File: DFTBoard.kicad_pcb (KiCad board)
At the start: 2 copper layers, 271 parts, among them CON1 AVR-JTAG-10, CON2 AVR-JTAG-10, IC1 WM8758B, IC2 IS31FL3199, IC3 CyUSB30xx-BZX, J1 JACK_TRS_6PINS, J2 JACK_TRS_6PINS, J3 JACK_TRS_6PINS, J4 JACK_TRS_6PINS, J5 MICRO_HDMI, J6 GSB3211311WEU, J7 48258-0001, Q1 IRLML2502, Q2 IRLML2502, Q3 IRLML2502, Q4 IRLML2502, Q5 IRLML2502, U1 xc7a50tftg256, U10 MAX3421, U11 GTL2002, U12 NC7WZ07P6X, U13 NC7SZ125M5X, U14 ADP198ACPZ-R7, U2 24FC128, U3 N25Q128A, U5 SC189 - 3.3V, U6 SC189 - 1.0V, U7 SC189 - 1.2V, U8 SC189 - 1.8V, U9 VL53L0X, X1 KC5032A, Y1 19.2MHz, Y2 12MHz

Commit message: a few small changes
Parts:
- moved J4 67.6 mm to (148.5, 105.0)
- moved J2 58.3 mm to (148.5, 105.0)
- moved ROT4 56.7 mm to (148.5, 105.0)
- moved J7 48.4 mm to (148.5, 105.0), turned to 0 degrees
- moved Y2 48.2 mm to (148.5, 105.0)
- moved J1 47.4 mm to (148.5, 105.0)
- moved ROT3 45.3 mm to (148.5, 105.0)
- moved C12 38.0 mm to (148.5, 105.0)
- moved ROT2 33.9 mm to (148.5, 105.0)
- moved DS1 33.8 mm to (148.5, 105.0)
- moved C21 33.3 mm to (148.5, 105.0)
- moved J3 30.6 mm to (148.5, 105.0)
- moved C24 25.0 mm to (148.5, 105.0)
- moved J6 24.0 mm to (148.5, 105.0)
- moved ROT1 22.5 mm to (148.5, 105.0)
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
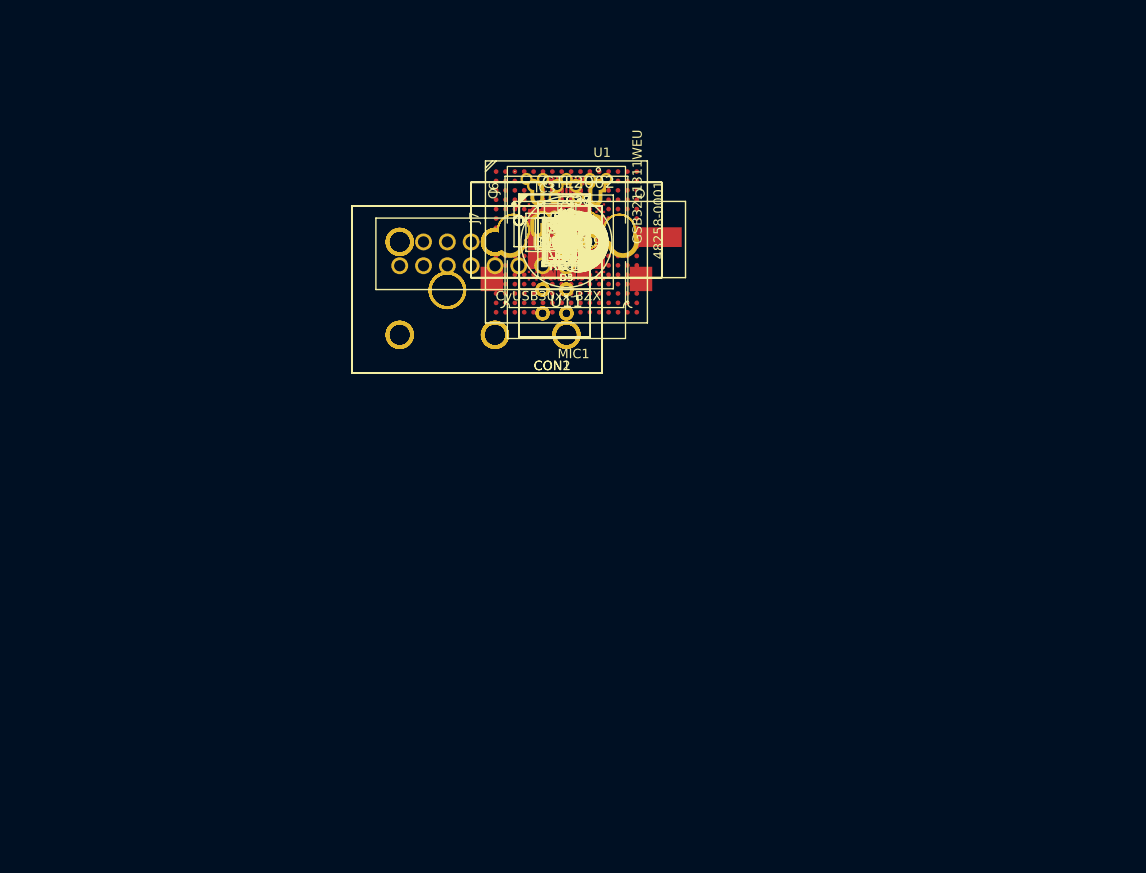
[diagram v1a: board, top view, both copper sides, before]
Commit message: fixed all schematic/footprint errors
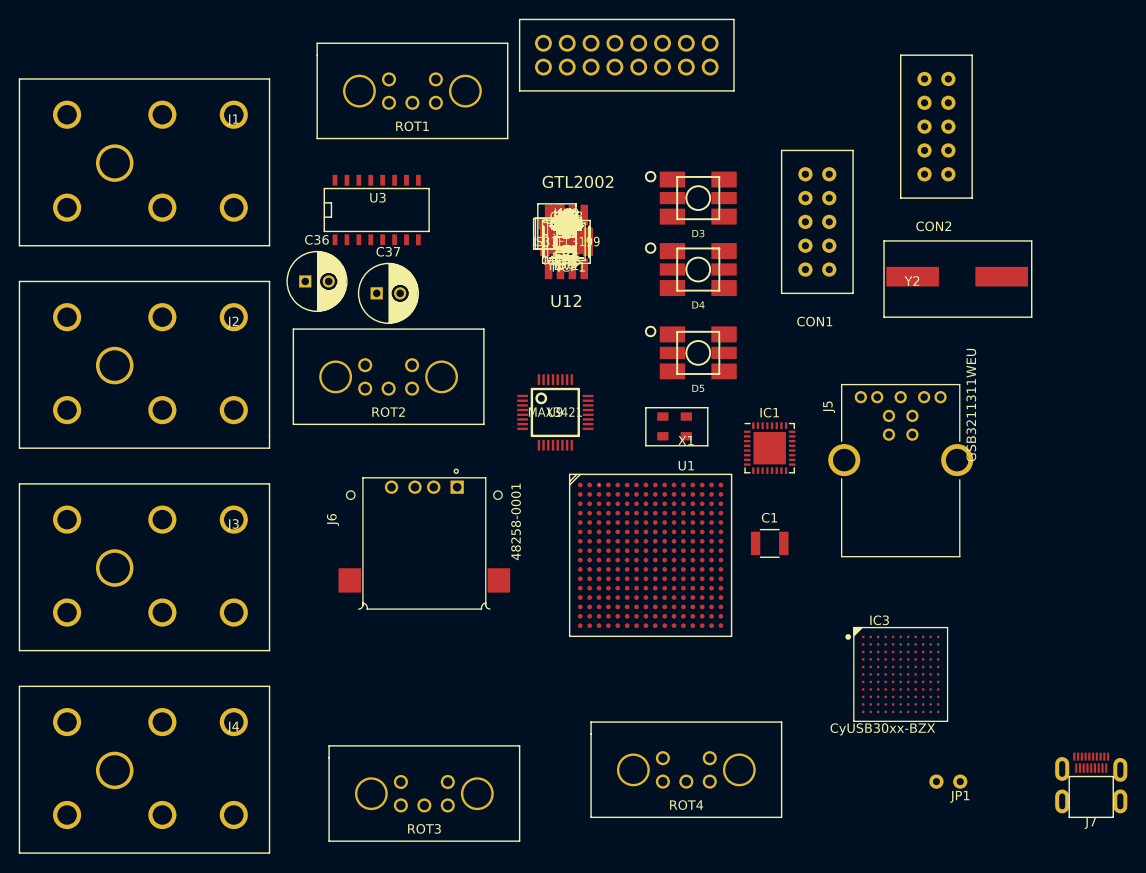
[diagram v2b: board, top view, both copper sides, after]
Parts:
- removed C126: 100nF, Capacitors_SMD:C_0603
- removed FB5: FERRITE, Diodes_SMD:D_0603
- removed R85, R86: 200, Resistors_SMD:R_1206
- removed U14: ADP198ACPZ-R7, DFTcustom:WLCSP4_P0.5mm
- added FB2: FERRITE, Diodes_SMD:D_0603, F.Cu at (148.5, 105.0)
- added U4: SC189 - 3.3V, TO_SOT_Packages_SMD:SOT-23-5, F.Cu at (148.5, 105.0)
- C100, C104: value 1uF -> .1uF
- C101: value .1uF -> 22pF; footprint Capacitors_SMD:C_0603 -> Capacitors_SMD:C_0201
- C103: value 22pF -> 1uF; footprint Capacitors_SMD:C_0201 -> Capacitors_SMD:C_0603
- C105: value .1uF -> 100nF
- C107: value 100nF -> 1nF, 250V
- C108: value 1nF, 250V -> 47uF; footprint Capacitors_SMD:C_0603 -> Capacitors_SMD:C_1210
- C109: value 47uF -> 4.7uF; footprint Capacitors_SMD:C_1210 -> Capacitors_SMD:C_0805
- C111: value 4.7uF -> .47uF; footprint Capacitors_SMD:C_0805 -> Capacitors_SMD:C_0603
- C115: value .47uF -> 100nF
- C26: value 220pF -> 4.7uF; footprint Capacitors_SMD:C_0201 -> Capacitors_SMD:C_0805
- C27, C28: value 1uF -> 4.7uF; footprint Capacitors_SMD:C_0603 -> Capacitors_SMD:C_0805
- C30: value 4.7uF -> .1uF
- C31: value .1uF -> 4.7uF
- C36: value 4.7uF -> 220uF; footprint Capacitors_SMD:C_0805 -> Capacitors_ThroughHole:C_Radial_D6.3_L11.2_P2.5
- C38: value 220uF -> .1uF; footprint Capacitors_ThroughHole:C_Radial_D6.3_L11.2_P2.5 -> Capacitors_SMD:C_0805
- C41: value .1uF -> .22uF; footprint Capacitors_SMD:C_0805 -> Capacitors_SMD:C_0402
- C43: value .22uF -> .1uF; footprint Capacitors_SMD:C_0402 -> Capacitors_SMD:C_0603
- C47, C49, C59, C70, C76, C78, C80, C84, C86: value .1uF -> .01uF; footprint Capacitors_SMD:C_0603 -> Capacitors_SMD:C_0402
- C48, C50, C60, C66, C77, C79, C85: value .01uF -> .1uF; footprint Capacitors_SMD:C_0402 -> Capacitors_SMD:C_0603
- C51: value .1uF -> 15pF; footprint Capacitors_SMD:C_0603 -> Capacitors_SMD:C_0402
- C53: value 15pF -> 2.2uF
- C54: value 2.2uF -> 22uF; footprint Capacitors_SMD:C_0402 -> Capacitors_SMD:C_0603
- C57: value 22uF -> .1uF
- C64: value .1uF -> 22uF
- C65, C74: value 22uF -> .01uF; footprint Capacitors_SMD:C_0603 -> Capacitors_SMD:C_0402
- C72, C73: value .01uF -> 0.1uF; footprint Capacitors_SMD:C_0402 -> Capacitors_SMD:C_0603
- C75: value .01uF -> 22uF; footprint Capacitors_SMD:C_0402 -> Capacitors_SMD:C_0603
- C82, C83: value 0.1uF -> .1uF
- C87: value .01uF -> 2.2uF
- C88: value 2.2uF -> .1uF; footprint Capacitors_SMD:C_0402 -> Capacitors_SMD:C_0603
- C89: value .1uF -> 10uF; footprint Capacitors_SMD:C_0603 -> Capacitors_SMD:C_0805
- C97: value 10uF -> 100nF; footprint Capacitors_SMD:C_0805 -> Capacitors_SMD:C_0603
- C98: value 100nF -> 4.7uF; footprint Capacitors_SMD:C_0603 -> Capacitors_SMD:C_0805
- C99: value 4.7uF -> 1uF; footprint Capacitors_SMD:C_0805 -> Capacitors_SMD:C_0603
- D6: value BAS16XV2T1G -> LED RED; footprint Diodes_SMD:SOD-523 -> LEDs:LED_0603
- D7: value LED RED -> LED BLUE
- D8: value LED BLUE -> BAS16XV2T1G; footprint LEDs:LED_0603 -> Diodes_SMD:SOD-523
- J1, J2, J3, J4: value JACK_TRS_6PINS -> JACK_TRS_5PINS
- J5: value MICRO_HDMI -> GSB3211311WEU; footprint DFTcustom:MICRO HDMI -> GSB3211311WEU:AMPHENOL_GSB3211311WEU
- J6: value GSB3211311WEU -> 48258-0001; footprint GSB3211311WEU:AMPHENOL_GSB3211311WEU -> 48258-0001:MOLEX_48258-0001
- J7: value 48258-0001 -> MICRO_HDMI; footprint 48258-0001:MOLEX_48258-0001 -> DFTcustom:MICRO_HDMI
- MIC1: value CMI-5247TF-K -> MEMSMIC; footprint DFTcustom:CMI-5247TF-K -> DFTcustom:WM7121PE
- NCP1: footprint UDFN-6:UDFN-6 -> DFTcustom:TSOP-5
- R2: value 270 -> 200
- R22: value 47K -> 22
- R23: value 680 -> 22
- R26: value 100k -> 50k
- R29: value 49.9k -> 100k
- R32: value 100k -> 49.9k
- R33: value 4.7k -> 100k
- R34: value 4.7k -> 50k
- R35: value 1k -> 50k
- R36: value 37.5 -> 20k
- R37: value 6.04k -> 4.7k
- R38: value 200 -> 4.7k
- R4: value 22 -> 270
- R40, R55, R58, R61: value 10k -> 1k
- R41: value 33 -> 37.5
- R42: value 33 -> 50k
- R43: value 20k -> 6.04k
- R44: value 1k -> 200
- R45, R77, R79: value 1k -> 10k
- R46: value 100k -> 10k
- R47: value 1MEG -> 1k
- R48: value 1k -> 145
- R49: value 27k -> 1k
- R5: value 22 -> 200
- R50: value 200k -> 90
- R51: value 1k -> 33
- R52: value 1.5k -> 33
- R53: value 1.5k -> 20k
- R54: value 100k -> 1k
- R56, R64: value 10k -> 100k
- R57: value 10k -> 1MEG
- R59: value 10k -> 27k
- R60: value 10k -> 200k
- R62, R63: value 10k -> 1.5k
- R75: value 20k -> 10k
- R76, R81, R82, R83: value 50k -> 10k
- R78: value 145 -> 10k
- R80: value 90 -> 10k
- U10: value MAX3421 -> NC7WZ07P6X; footprint TQFP32-5MM:TQFP32-5MM -> DFTcustom:SC-70-6
- U11: value GTL2002 -> NC7SZ125M5X; footprint DFTcustom:SO-8 -> DFTcustom:SOT-23-5
- U12: value NC7WZ07P6X -> GTL2002; footprint TO_SOT_Packages_SMD:SC-70 -> DFTcustom:SO-8
- U13: value NC7SZ125M5X -> ADP198ACPZ-R7; footprint TO_SOT_Packages_SMD:SOT-23 -> DFTcustom:LFCSP_UD
- U3: footprint DFTcustom:V-PDFN-8 6mmx5mm Sawm (MLP8) -> SMD_Packages:SO-16-N
- U5: value SC189 - 3.3V -> SC189 - 1.0V
- U6: value SC189 - 1.0V -> SC189 - 1.2V
- U7: value SC189 - 1.2V -> SC189 - 1.8V
- U8: value SC189 - 1.8V -> VL53L0X; footprint TO_SOT_Packages_SMD:SOT-23-5 -> DFTcustom:LGA12
- U9: value VL53L0X -> MAX3421; footprint DFTcustom:LGA12 -> TQFP32-5MM:TQFP32-5MM
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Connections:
- C101 pad 1: +1.8V -> AGND
- C101 pad 2: AGND -> Net-(C101-Pad2)
- C103 pad 1: AGND -> +3V3
- C103 pad 2: Net-(C103-Pad2) -> AGND
- C106 pad 1: +3V3 -> Net-(C106-Pad1)
- C107 pad 1: Net-(C107-Pad1) -> AGND
- C107 pad 2: AGND -> Net-(C107-Pad2)
- C108 pad 1: AGND -> +3V3
- C108 pad 2: Net-(C108-Pad2) -> AGND
- C26 pad 1: AGND -> Net-(C26-Pad1)
- C27 pad 1: Net-(C26-Pad2) -> +3V3
- C27 pad 2: Net-(C27-Pad2) -> AGND
- C30 pad 1: +3V3 -> JD_IN
- C31 pad 1: JD_IN -> +1.8V
- C33 pad 1: +1.8V -> Net-(C33-Pad1)
- C34 pad 2: Net-(C34-Pad2) -> AGND
- C36 pad 1: MICBIAS -> Net-(C36-Pad1)
- C36 pad 2: AGND -> Net-(C36-Pad2)
- C38 pad 1: Net-(C38-Pad1) -> JD_ROUT
- C38 pad 2: Net-(C38-Pad2) -> AGND
- C39 pad 1: JD_ROUT -> JD_LOUT
- C40 pad 1: JD_LOUT -> JD_HOUT
- C41 pad 1: JD_HOUT -> Net-(C41-Pad1)
- C41 pad 2: AGND -> AUDIO_IN
- C43 pad 1: Net-(C43-Pad1) -> +3V3
- C43 pad 2: AUDIO_IN -> AGND
- C44 pad 1: +3V3 -> Net-(C44-Pad1)
- C45 pad 1: Net-(C45-Pad1) -> +5V
- C47 pad 1: +5V -> +1.8V
- C51 pad 1: +1.8V -> Net-(C51-Pad1)
- C53 pad 1: Net-(C53-Pad1) -> +1.2V
- C57 pad 1: +1.2V -> CVDDQ
- C58 pad 1: CVDDQ -> +1.2V
- C59 pad 1: +1.2V -> CVDDQ
- C60 pad 1: CVDDQ -> +1.2V
- C61 pad 1: +1.2V -> Net-(C61-Pad1)
- C62 pad 1: Net-(C62-Pad1) -> +1.8V
- C63 pad 1: +1.8V -> +1.2V
- C64 pad 1: +1.2V -> Net-(C61-Pad1)
- C65 pad 1: Net-(C62-Pad1) -> +1.8V
- C66 pad 1: +1.8V -> +1.2V
- C67 pad 1: +1.2V -> +3V3
- C68 pad 1: +3V3 -> Net-(C68-Pad1)
- C69 pad 1: Net-(C69-Pad1) -> +1.8V
- C70 pad 1: +1.8V -> +1.2V
- C71 pad 1: +1.2V -> +3V3
- C72 pad 1: +3V3 -> Net-(C72-Pad1)
- C72 pad 2: AGND -> Net-(C72-Pad2)
- C73 pad 1: +1.2V -> Net-(C73-Pad1)
- C73 pad 2: AGND -> Net-(C73-Pad2)
- C74 pad 1: Net-(C69-Pad1) -> +1.2V
- C75 pad 1: +1.8V -> Net-(C68-Pad1)
- C77 pad 1: +1.2V -> +1.8V
- C78 pad 1: +1.8V -> +1.2V
- C80 pad 1: +1.2V -> +1.8V
- C81 pad 1: Net-(C81-Pad1) -> +1.2V
- C82 pad 2: Net-(C82-Pad2) -> AGND
- C83 pad 1: Net-(C83-Pad1) -> +5V
- C83 pad 2: Net-(C83-Pad2) -> AGND
- C84 pad 1: +5V -> +1.8V
- C86 pad 1: +1.8V -> +1.2V
- C87 pad 1: +1.2V -> Net-(C82-Pad1)
- C88 pad 1: Net-(C81-Pad1) -> +1.2V
- C89 pad 1: +1.2V -> +5V
- C91 pad 1: +5V -> +3V3
- C92 pad 1: +3V3 -> +1.0V
- C93 pad 1: +1.0V -> +5V
- C95 pad 1: +5V -> +1.2V
- C96 pad 1: +1.2V -> +1.8V
- C97 pad 1: +1.8V -> +3V3
- C99 pad 1: +3V3 -> +1.8V
- F1 pad 1: (no net) -> Net-(F1-Pad1)
- F1 pad 2: (no net) -> HDMI_5V0
- FB3 pad 2: Net-(C62-Pad1) -> Net-(C68-Pad1)
- FB4 pad 2: Net-(C69-Pad1) -> Net-(C82-Pad1)
- IC1 pad 19: Net-(IC1-Pad19) -> Net-(C33-Pad1)
- IC1 pad 20: Net-(C34-Pad2) -> Net-(C28-Pad2)
- IC1 pad 23: Net-(C38-Pad1) -> Net-(C37-Pad1)
- IC1 pad 25: Net-(C37-Pad1) -> Net-(C36-Pad1)
- IC1 pad 27: Net-(C35-Pad1) -> Net-(C34-Pad1)
- IC1 pad 32: MICBIAS -> Net-(C35-Pad1)
- IC1 pad 4: Net-(C27-Pad2) -> Net-(C26-Pad1)
- IC1 pad 5: Net-(C28-Pad2) -> AGND
- IC2 pad 17: Net-(C43-Pad1) -> Net-(C41-Pad1)
- IC2 pad 2: Net-(C45-Pad1) -> Net-(C44-Pad1)
- IC3 pad A2: Net-(C62-Pad1) -> Net-(C61-Pad1)
- IC3 pad A5: Net-(C83-Pad2) -> Net-(C73-Pad2)
- IC3 pad A6: Net-(C82-Pad2) -> Net-(C72-Pad2)
- IC3 pad A7: Net-(C81-Pad1) -> Net-(C82-Pad1)
- IC3 pad B5: Net-(C69-Pad1) -> Net-(C68-Pad1)
- IC3 pad C6: Net-(C52-Pad1) -> Net-(C51-Pad1)
- IC3 pad C7: Net-(C53-Pad1) -> Net-(C52-Pad1)
- J1 pad R: (no net) -> Net-(IC1-Pad2)
- J1 pad RB: (no net) -> Net-(IC1-Pad2)
- J1 pad S: (no net) -> AGND
- J1 pad T: (no net) -> Net-(IC1-Pad1)
- J1 pad TB: (no net) -> Net-(J1-PadTB)
- J2 pad R: (no net) -> Net-(C37-Pad2)
- J2 pad RB: (no net) -> Net-(J2-PadRB)
- J2 pad S: (no net) -> AGND
- J2 pad T: (no net) -> Net-(C36-Pad2)
- J2 pad TB: (no net) -> Net-(C36-Pad2)
- J3 pad R: (no net) -> AGND
- J3 pad RB: (no net) -> AGND
- J3 pad S: (no net) -> AGND
- J3 pad T: (no net) -> Net-(IC1-Pad29)
- J3 pad TB: (no net) -> Net-(J3-PadTB)
- J4 pad R: (no net) -> AGND
- J4 pad RB: (no net) -> AGND
- J4 pad S: (no net) -> AGND
- J4 pad T: (no net) -> Net-(IC1-Pad30)
- J4 pad TB: (no net) -> Net-(J4-PadTB)
- J5 pad 1: Net-(J5-Pad1) -> +5V
- J5 pad 2: Net-(J5-Pad2) -> Net-(IC3-PadA10)
- J5 pad 3: Net-(J5-Pad3) -> Net-(IC3-PadA9)
- J5 pad 5: Net-(J5-Pad5) -> Net-(C72-Pad1)
- J5 pad 6: Net-(J5-Pad6) -> Net-(C73-Pad1)
- J5 pad 8: Net-(J5-Pad8) -> Net-(IC3-PadA3)
- J5 pad 9: Net-(J5-Pad9) -> Net-(IC3-PadA4)
- J6 pad 1: +5V -> Net-(J6-Pad1)
- J6 pad 2: Net-(IC3-PadA10) -> Net-(J6-Pad2)
- J6 pad 3: Net-(IC3-PadA9) -> Net-(J6-Pad3)
- MIC1 pad 1: AGND -> +3V3
- MIC1 pad 2: Net-(C26-Pad2) -> AGND
- Q1 pad 2: AGND -> Net-(Q1-Pad2)
- Q1 pad 3: Net-(DS1-Pad16) -> +3V3
- Q2 pad 2: AGND -> Net-(Q2-Pad2)
- Q2 pad 3: Net-(D7-Pad1) -> +3V3
- Q3 pad 3: Net-(D8-Pad1) -> Net-(DS1-Pad16)
- Q4 pad 2: Net-(Q4-Pad2) -> AGND
- Q4 pad 3: +3V3 -> Net-(D6-Pad1)
- Q5 pad 2: Net-(Q5-Pad2) -> AGND
- Q5 pad 3: +3V3 -> Net-(D7-Pad1)
- R1 pad 2: Net-(Q4-Pad2) -> Net-(Q1-Pad2)
- R10 pad 2: GD_10 -> GD_2
- R11 pad 2: GD_14 -> GD_6
- R12 pad 2: GA_1 -> GD_10
- R13 pad 2: GD_1 -> GD_14
- R14 pad 2: GD_5 -> GA_1
- R15 pad 2: GD_9 -> GD_1
- R16 pad 2: GD_13 -> GD_5
- R17 pad 2: GA_0 -> GD_9
- R18 pad 2: GD_0 -> GD_13
- R19 pad 2: GD_4 -> GA_0
- R2 pad 1: Net-(D2-Pad2) -> Net-(Q1-Pad1)
- R2 pad 2: Net-(Q5-Pad2) -> CONFIG_DONE
- R20 pad 2: GD_8 -> GD_0
- R21 pad 2: GD_12 -> GD_4
- R22 pad 1: Net-(C26-Pad2) -> Net-(R22-Pad1)
- R22 pad 2: AGND -> GD_8
- R23 pad 1: MICBIAS -> Net-(R23-Pad1)
- R23 pad 2: Net-(C26-Pad2) -> GD_12
- R24 pad 2: Net-(J1-Pad5) -> Net-(J1-PadTB)
- R25 pad 2: Net-(J1-Pad5) -> Net-(J1-PadTB)
- R26 pad 1: Net-(J2-Pad5) -> +1.8V
- R26 pad 2: +3V3 -> Net-(IC1-Pad15)
- R27 pad 1: Net-(J3-Pad5) -> Net-(J3-PadTB)
- R28 pad 1: Net-(J4-Pad6) -> Net-(J4-PadTB)
- R29 pad 1: JD_ROUT -> Net-(J2-PadRB)
- R29 pad 2: Net-(J2-Pad5) -> +3V3
- R30 pad 1: JD_LOUT -> JD_ROUT
- R30 pad 2: Net-(J3-Pad5) -> Net-(J3-PadTB)
- R31 pad 1: JD_HOUT -> JD_LOUT
- R31 pad 2: Net-(J4-Pad6) -> Net-(J4-PadTB)
- R32 pad 1: Net-(IC2-Pad15) -> JD_HOUT
- R32 pad 2: AGND -> Net-(J2-PadRB)
- R33 pad 1: I2C_SCLK -> Net-(IC2-Pad15)
- R33 pad 2: +1.8V -> AGND
- R34 pad 1: I2C_SDIN -> Net-(IC2-Pad16)
- R34 pad 2: +1.8V -> AGND
- R35 pad 1: Net-(Q1-Pad1) -> Net-(R35-Pad1)
- R35 pad 2: PWM_LCD_DIM -> +1.8V
- R36 pad 1: Net-(DS1-Pad15) -> +1.8V
- R36 pad 2: +5V -> Net-(R36-Pad2)
- R37 pad 1: Net-(IC3-PadC8) -> I2C_SCLK
- R37 pad 2: AGND -> +1.8V
- R38 pad 1: Net-(IC3-PadB3) -> I2C_SDIN
- R38 pad 2: AGND -> +1.8V
- R39 pad 2: RF_SD -> Net-(IC3-PadH4)
- R4 pad 1: Net-(R4-Pad1) -> Net-(D2-Pad2)
- R4 pad 2: GD_3 -> Net-(Q2-Pad2)
- R40 pad 1: +1.8V -> Net-(Q3-Pad1)
- R40 pad 2: RF_IRQ -> PWM_LCD_DIM
- R41 pad 1: Net-(J7-Pad2) -> Net-(DS1-Pad15)
- R41 pad 2: Net-(R41-Pad2) -> +5V
- R42 pad 1: Net-(J7-Pad3) -> CVDDQ
- R42 pad 2: Net-(R42-Pad2) -> Net-(IC3-PadC5)
- R43 pad 1: +5V -> Net-(IC3-PadC8)
- R43 pad 2: USB_FAULT -> AGND
- R44 pad 1: +3V3 -> Net-(IC3-PadB3)
- R44 pad 2: HDMI_SCL -> AGND
- R45 pad 1: +3V3 -> +1.8V
- R45 pad 2: HDMI_SDA -> RF_SD
- R46 pad 1: Net-(J5-Pad1) -> +1.8V
- R46 pad 2: AGND -> RF_IRQ
- R47 pad 1: AGND -> Net-(Q4-Pad1)
- R47 pad 2: Net-(C108-Pad2) -> Net-(R47-Pad2)
- R48 pad 1: Net-(R48-Pad1) -> Net-(D6-Pad2)
- R48 pad 2: Net-(J5-Pad1) -> +5V
- R49 pad 1: Net-(D6-Pad1) -> Net-(Q5-Pad1)
- R49 pad 2: +3V3 -> Net-(R49-Pad2)
- R5 pad 1: Net-(R5-Pad1) -> Net-(Q2-Pad1)
- R5 pad 2: GD_7 -> CONFIG_INIT
- R50 pad 1: HDMI_5V0 -> Net-(D7-Pad2)
- R50 pad 2: Net-(C107-Pad1) -> +5V
- R51 pad 1: Net-(R51-Pad1) -> Net-(J6-Pad2)
- R52 pad 1: HDMI_5V0 -> Net-(J6-Pad3)
- R52 pad 2: Net-(J5-Pad17) -> Net-(R52-Pad2)
- R53 pad 1: HDMI_5V0 -> +5V
- R53 pad 2: Net-(J5-Pad18) -> USB_FAULT
- R54 pad 1: Net-(R51-Pad1) -> +3V3
- R54 pad 2: AGND -> HDMI_SCL
- R55 pad 1: +1.8V -> +3V3
- R55 pad 2: ENCC0_SW -> HDMI_SDA
- R56 pad 1: +1.8V -> Net-(J7-Pad1)
- R56 pad 2: ENCC2_SW -> AGND
- R57 pad 1: +1.8V -> AGND
- R57 pad 2: Net-(R57-Pad2) -> Net-(C107-Pad2)
- R58 pad 1: +1.8V -> Net-(R58-Pad1)
- R58 pad 2: Net-(R58-Pad2) -> Net-(J7-Pad1)
- R59 pad 1: +1.8V -> Net-(D8-Pad1)
- R59 pad 2: Net-(R59-Pad2) -> +3V3
- R6 pad 2: GD_11 -> GD_3
- R60 pad 1: +1.8V -> HDMI_5V0
- R60 pad 2: Net-(R60-Pad2) -> Net-(C106-Pad1)
- R61 pad 1: ENCC0_Q0 -> Net-(R61-Pad1)
- R61 pad 2: Net-(R57-Pad2) -> Net-(R61-Pad2)
- R62 pad 1: ENCC0_Q1 -> HDMI_5V0
- R62 pad 2: Net-(R59-Pad2) -> Net-(J7-Pad17)
- R63 pad 1: ENCC2_Q0 -> HDMI_5V0
- R63 pad 2: Net-(R58-Pad2) -> Net-(J7-Pad18)
- R64 pad 1: ENCC2_Q1 -> Net-(R61-Pad1)
- R64 pad 2: Net-(R60-Pad2) -> AGND
- R65 pad 2: ENCC1_SW -> ENCC0_SW
- R66 pad 1: +3V3 -> +1.8V
- R66 pad 2: ENCC3_SW -> ENCC2_SW
- R68 pad 1: +3V3 -> +1.8V
- R7 pad 2: GD_15 -> GD_7
- R70 pad 1: +3V3 -> +1.8V
- R71 pad 1: ENCC1_Q0 -> ENCC0_Q0
- R72 pad 1: ENCC1_Q1 -> ENCC0_Q1
- R73 pad 1: ENCC3_Q0 -> ENCC2_Q0
- R74 pad 1: ENCC3_Q1 -> ENCC2_Q1
- R75 pad 2: Net-(R75-Pad2) -> ENCC1_SW
- R76 pad 1: CVDDQ -> +3V3
- R76 pad 2: Net-(IC3-PadC5) -> ENCC3_SW
- R77 pad 1: Net-(Q2-Pad1) -> +1.8V
- R78 pad 1: Net-(D7-Pad2) -> +3V3
- R78 pad 2: +5V -> Net-(R78-Pad2)
- R79 pad 1: Net-(Q3-Pad1) -> +1.8V
- R8 pad 2: GD_2 -> GD_11
- R80 pad 1: Net-(D8-Pad2) -> +3V3
- R80 pad 2: +5V -> Net-(R80-Pad2)
- R81 pad 1: +1.8V -> ENCC1_Q0
- R81 pad 2: Net-(IC1-Pad15) -> Net-(R77-Pad2)
- R82 pad 1: Net-(R82-Pad1) -> ENCC1_Q1
- R82 pad 2: +1.8V -> Net-(R79-Pad2)
- R83 pad 1: Net-(IC2-Pad16) -> ENCC3_Q0
- R83 pad 2: AGND -> Net-(R78-Pad2)
- R84 pad 1: +1.8V -> ENCC3_Q1
- R84 pad 2: Net-(IC3-PadH4) -> Net-(R80-Pad2)
- R9 pad 2: GD_6 -> GD_15
- ROT1 pad A: (no net) -> Net-(R67-Pad2)
- ROT1 pad B: (no net) -> Net-(R69-Pad2)
- ROT1 pad C: (no net) -> AGND
- ROT1 pad S1: (no net) -> ENCC0_SW
- ROT1 pad S2: (no net) -> AGND
- ROT2 pad A: (no net) -> Net-(R68-Pad2)
- ROT2 pad B: (no net) -> Net-(R70-Pad2)
- ROT2 pad C: (no net) -> AGND
- ROT2 pad S1: (no net) -> ENCC2_SW
- ROT2 pad S2: (no net) -> AGND
- ROT3 pad A: (no net) -> Net-(R77-Pad2)
- ROT3 pad B: (no net) -> Net-(R79-Pad2)
- ROT3 pad C: (no net) -> AGND
- ROT3 pad S1: (no net) -> ENCC1_SW
- ROT3 pad S2: (no net) -> AGND
- ROT4 pad A: (no net) -> Net-(R78-Pad2)
- ROT4 pad B: (no net) -> Net-(R80-Pad2)
- ROT4 pad C: (no net) -> AGND
- ROT4 pad S1: (no net) -> ENCC3_SW
- ROT4 pad S2: (no net) -> AGND
- U1 pad A3: Net-(J5-Pad11) -> Net-(J7-Pad11)
- U1 pad A7: Net-(J5-Pad8) -> Net-(J7-Pad8)
- U1 pad B4: Net-(J5-Pad9) -> Net-(J7-Pad9)
- U1 pad B5: Net-(J5-Pad5) -> Net-(J7-Pad5)
- U1 pad B6: Net-(J5-Pad3) -> Net-(J7-Pad3)
- U1 pad B7: Net-(J5-Pad6) -> Net-(J7-Pad6)
- U1 pad C6: Net-(D6-Pad2) -> Net-(D8-Pad2)
- U1 pad C7: Net-(R51-Pad1) -> Net-(R61-Pad1)
- U1 pad E5: Net-(J5-Pad14) -> Net-(J7-Pad14)
- U1 pad F5: Net-(J5-Pad12) -> Net-(J7-Pad12)
- U1 pad K13: Net-(R5-Pad1) -> Net-(R7-Pad1)
- U1 pad K15: Net-(R13-Pad1) -> Net-(R15-Pad1)
- U1 pad K16: Net-(R18-Pad1) -> Net-(R20-Pad1)
- U1 pad L12: Net-(R15-Pad1) -> Net-(R17-Pad1)
- U1 pad L13: Net-(R9-Pad1) -> Net-(R11-Pad1)
- U1 pad L14: Net-(R14-Pad1) -> Net-(R16-Pad1)
- U1 pad L15: Net-(R4-Pad1) -> Net-(R6-Pad1)
- U1 pad M12: Net-(R20-Pad1) -> Net-(R22-Pad1)
- U1 pad M14: Net-(R19-Pad1) -> Net-(R21-Pad1)
- U1 pad M15: Net-(R8-Pad1) -> Net-(R10-Pad1)
- U1 pad M16: Net-(R6-Pad1) -> Net-(R8-Pad1)
- U1 pad N13: Net-(R12-Pad1) -> Net-(R14-Pad1)
- U1 pad N16: Net-(R10-Pad1) -> Net-(R12-Pad1)
- U1 pad P13: Net-(R17-Pad1) -> Net-(R19-Pad1)
- U1 pad P15: Net-(R16-Pad1) -> Net-(R18-Pad1)
- U1 pad P16: Net-(R21-Pad1) -> Net-(R23-Pad1)
- U1 pad R15: Net-(R7-Pad1) -> Net-(R9-Pad1)
- U1 pad R16: Net-(R11-Pad1) -> Net-(R13-Pad1)
- U10 pad 1: ENCC2_Q1 -> Net-(J7-Pad1)
- U10 pad 2: +1.8V -> AGND
- U10 pad 3: AGND -> Net-(U10-Pad3)
- U10 pad 4: LED_SD -> Net-(U10-Pad4)
- U10 pad 5: RF_SD -> +3V3
- U10 pad 6: I2CMEM_WP -> Net-(R61-Pad2)
- U11 pad 1: AGND -> HDMI_OUT_EN
- U11 pad 2: +3V3 -> Net-(R61-Pad1)
- U11 pad 3: HDMI_SCL -> AGND
- U11 pad 4: HDMI_SDA -> Net-(R58-Pad1)
- U11 pad 5: Net-(J5-Pad18) -> +3V3
- U12 pad 1: Net-(J5-Pad1) -> AGND
- U12 pad 2: (no net) -> +3V3
- U12 pad 3: (no net) -> HDMI_SCL
- U13 pad 1: HDMI_OUT_EN -> Net-(F1-Pad1)
- U13 pad 2: Net-(R51-Pad1) -> Net-(F1-Pad1)
- U13 pad 3: (no net) -> AGND
- U3 pad 1: Net-(R82-Pad1) -> Net-(R35-Pad1)
- U5 pad 4: +3V3 -> +1.0V
- U5 pad 5: Net-(L1-Pad1) -> Net-(L2-Pad1)
- U6 pad 4: +1.0V -> +1.2V
- U6 pad 5: Net-(L2-Pad1) -> Net-(L3-Pad1)
- U7 pad 4: +1.2V -> +1.8V
- U7 pad 5: Net-(L3-Pad1) -> Net-(L4-Pad1)
- U8 pad 1: +5V -> +3V3
- U8 pad 3: +5V -> AGND
- U8 pad 4: +1.8V -> AGND
- U8 pad 5: Net-(L4-Pad1) -> RF_SD
- U9 pad 1: +3V3 -> ENCC2_Q1
- U9 pad 10: I2C_SCLK -> Net-(R49-Pad2)
- U9 pad 11: +3V3 -> Net-(U9-Pad11)
- U9 pad 12: AGND -> +1.8V
- U9 pad 2: AGND -> +1.8V
- U9 pad 4: AGND -> LED_SD
- U9 pad 6: AGND -> I2CMEM_WP
- U9 pad 7: RF_IRQ -> CONFIG_INIT
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
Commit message: started PCBnew trivial connections and BGA interface, shuffled some net connections, etc.
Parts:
- removed C36, C37: 220uF, Capacitors_ThroughHole:C_Radial_D6.3_L11.2_P2.5
- removed D8: BAS16XV2T1G, Diodes_SMD:SOD-523
- added Q6: IRLML2502, TO_SOT_Packages_SMD:SOT-23, F.Cu at (74.8, 50.2)
- added R85: 10k, Resistors_SMD:R_1206, F.Cu at (142.2, 75.0)
- added R86: 10k, Resistors_SMD:R_1206, F.Cu at (137.8, 76.2)
- added R87: 10k, Resistors_SMD:R_1206, F.Cu at (148.3, 78.6)
- added R88: 10k, Resistors_SMD:R_1206, F.Cu at (135.1, 82.0)
- added R89: 10k, Resistors_SMD:R_1206, F.Cu at (141.2, 70.1)
- added R90: 10k, Resistors_SMD:R_1206, F.Cu at (127.2, 74.7)
- added R91: 10k, Resistors_SMD:R_1206, F.Cu at (134.6, 70.9)
- added R92: 10k, Resistors_SMD:R_1206, F.Cu at (141.8, 83.4)
- added R93: 10k, Resistors_SMD:R_1206, F.Cu at (129.9, 79.8)
- added SW1: SW_IL, DFTcustom:tl6215_right_angle, F.Cu at (74.0, 38.5)
- C10, C11, C12, C13, C14, C15, C16, C17, C18, C19, C20, C21, C22, C23, C24, C25, C9, DS1, NCP1, U9: moved to B.Cu
- C63: value .1uF -> 0.1uF
- C64: value 22uF -> 0.1uF
- C65, C70, C71: value .01uF -> .1uF; footprint Capacitors_SMD:C_0402 -> Capacitors_SMD:C_0603
- C66: value .1uF -> 22uF
- C67: value .1uF -> .01uF; footprint Capacitors_SMD:C_0603 -> Capacitors_SMD:C_0402
- C72, C73: value 0.1uF -> .01uF; footprint Capacitors_SMD:C_0603 -> Capacitors_SMD:C_0402
- IC3: footprint CYUSB3014-BZXCT:BGA121C80P11X11_1000X1000X110 -> DFTcustom:BGA121_08mm
- R1: value 60 -> 200
- R10, R11, R12, R13, R14, R15, R16, R17, R18, R19, R20, R21, R22, R23, R6, R7, R8, R9: footprint Resistors_SMD:R_1206 -> Resistors_SMD:R_0201
- R2: value 200 -> 60
- R24, R27, R28, R29: value 100k -> 22; footprint Resistors_SMD:R_1206 -> Resistors_SMD:R_0201
- R25, R30, R31: value 49.9k -> 22; footprint Resistors_SMD:R_1206 -> Resistors_SMD:R_0201
- R26: value 50k -> 22; footprint Resistors_SMD:R_1206 -> Resistors_SMD:R_0201
- R3: value 4.7k -> 270
- R32: value 49.9k -> 100k
- R33: value 100k -> 49.9k
- R35: value 50k -> 100k
- R36: value 20k -> 100k
- R37: value 4.7k -> 100k
- R38: value 4.7k -> 49.9k
- R39: value 10k -> 49.9k
- R4: value 270 -> 200
- R40: value 1k -> 49.9k
- R41: value 37.5 -> 100k
- R43: value 6.04k -> 50k
- R44: value 200 -> 20k
- R45, R46: value 10k -> 4.7k
- R47, R54: value 1k -> 10k
- R48: value 145 -> 1k
- R49: value 1k -> 37.5
- R5: value 200 -> 4.7k
- R50: value 90 -> 50k
- R51: value 33 -> 6.04k
- R52: value 33 -> 200
- R53: value 20k -> 10k
- R56: value 100k -> 145
- R57: value 1MEG -> 1k
- R58: value 1k -> 90
- R59: value 27k -> 20k
- R60: value 200k -> 33; moved to B.Cu
- R61: value 1k -> 33; moved to B.Cu
- R62: value 1.5k -> 20k
- R63: value 1.5k -> 1k
- R64: value 100k -> 1k
- R65, R73: value 10k -> 100k
- R66: value 10k -> 1MEG
- R67, R70: value 10k -> 1k
- R68: value 10k -> 27k
- R69: value 10k -> 200k
- R71, R72: value 10k -> 1.5k
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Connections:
- net Net-(C51-Pad1) renamed /Cypress FX3/XP
- net Net-(C52-Pad1) renamed /Cypress FX3/XN
- net Net-(C82-Pad1) renamed /Cypress FX3/AVDD
- net Net-(CON1-Pad1) renamed AX_TCLK
- net Net-(CON1-Pad3) renamed AX_TDO
- net Net-(CON1-Pad5) renamed AX_TMS
- net Net-(CON1-Pad9) renamed AX_TDI
- net Net-(CON2-Pad1) renamed FX_TCK
- net Net-(CON2-Pad3) renamed FX_TDO
- net Net-(CON2-Pad5) renamed FX_TMS
- net Net-(CON2-Pad8) renamed FX_nTRST
- net Net-(CON2-Pad9) renamed FX_TDI
- net Net-(D8-Pad2) renamed HDMI_CEC
- net Net-(DS1-Pad11) renamed LCD_D4
- net Net-(DS1-Pad12) renamed LCD_D5
- net Net-(DS1-Pad13) renamed LCD_D6
- net Net-(DS1-Pad14) renamed LCD_D7
- net Net-(DS1-Pad4) renamed LCD_RS
- net Net-(DS1-Pad6) renamed LCD_E
- net Net-(IC3-PadA10) renamed FXD_N
- net Net-(IC3-PadA9) renamed FXD_P
- net Net-(J6-Pad1) renamed SPIUSB_VBUS
- net Net-(J7-Pad11) renamed TMDS_DAT0_N
- net Net-(J7-Pad12) renamed TMDS_CLK_P
- net Net-(J7-Pad14) renamed TMDS_CLK_N
- net Net-(J7-Pad3) renamed TMDS_DAT2_P
- net Net-(J7-Pad5) renamed TMDS_DAT2_N
- net Net-(J7-Pad6) renamed TMDS_DAT1_P
- net Net-(J7-Pad8) renamed TMDS_DAT1_N
- net Net-(J7-Pad9) renamed TMDS_DAT0_P
- C107 pad 2: Net-(C107-Pad2) -> /HDMI/HDMI_SHD
- C61 pad 1: Net-(C61-Pad1) -> /Cypress FX3/U3RXVDDQ
- C63 pad 1: +1.2V -> SSTX_N
- C63 pad 2: AGND -> /Cypress FX3/SSTXAC_N
- C64 pad 1: Net-(C61-Pad1) -> SSTX_P
- C64 pad 2: AGND -> /Cypress FX3/SSTXAC_P
- C65 pad 1: +1.8V -> +1.2V
- C66 pad 1: +1.2V -> /Cypress FX3/U3RXVDDQ
- C67 pad 1: +3V3 -> +1.8V
- C68 pad 1: Net-(C68-Pad1) -> +1.2V
- C69 pad 1: +1.8V -> +3V3
- C70 pad 1: +1.2V -> /Cypress FX3/U3TXVDDQ
- C71 pad 1: +3V3 -> +1.8V
- C72 pad 1: Net-(C72-Pad1) -> +1.2V
- C72 pad 2: Net-(C72-Pad2) -> AGND
- C73 pad 1: Net-(C73-Pad1) -> +3V3
- C73 pad 2: Net-(C73-Pad2) -> AGND
- C75 pad 1: Net-(C68-Pad1) -> /Cypress FX3/U3TXVDDQ
- CON1 pad 6: Net-(CON1-Pad6) -> (no net)
- CON1 pad 7: Net-(CON1-Pad7) -> (no net)
- CON1 pad 8: Net-(CON1-Pad8) -> (no net)
- CON2 pad 6: Net-(CON2-Pad6) -> (no net)
- CON2 pad 7: Net-(CON2-Pad7) -> (no net)
- D1 pad 1: AGND -> Net-(D1-Pad1)
- D2 pad 1: AGND -> Net-(D2-Pad1)
- DS1 pad 10: Net-(DS1-Pad10) -> (no net)
- DS1 pad 7: Net-(DS1-Pad7) -> (no net)
- DS1 pad 8: Net-(DS1-Pad8) -> (no net)
- DS1 pad 9: Net-(DS1-Pad9) -> (no net)
- FB2 pad 2: Net-(C61-Pad1) -> /Cypress FX3/U3RXVDDQ
- FB3 pad 2: Net-(C68-Pad1) -> /Cypress FX3/U3TXVDDQ
- IC1 pad 21: Net-(IC1-Pad21) -> (no net)
- IC1 pad 23: Net-(C37-Pad1) -> (no net)
- IC1 pad 25: Net-(C36-Pad1) -> (no net)
- IC1 pad 3: Net-(IC1-Pad3) -> (no net)
- IC1 pad 6: Net-(IC1-Pad6) -> (no net)
- IC2 pad 14: Net-(IC2-Pad14) -> (no net)
- IC2 pad 20: Net-(IC2-Pad20) -> (no net)
- IC3 pad A11: Net-(IC3-PadA11) -> (no net)
- IC3 pad A2: Net-(C61-Pad1) -> /Cypress FX3/U3RXVDDQ
- IC3 pad A3: Net-(IC3-PadA3) -> SSRX_N
- IC3 pad A4: Net-(IC3-PadA4) -> SSRX_P
- IC3 pad A5: Net-(C73-Pad2) -> /Cypress FX3/SSTXAC_P
- IC3 pad A6: Net-(C72-Pad2) -> /Cypress FX3/SSTXAC_N
- IC3 pad B3: Net-(IC3-PadB3) -> /Cypress FX3/RUSB3
- IC3 pad B5: Net-(C68-Pad1) -> /Cypress FX3/U3TXVDDQ
- IC3 pad C5: Net-(IC3-PadC5) -> /Cypress FX3/nRESET
- IC3 pad C8: Net-(IC3-PadC8) -> /Cypress FX3/RUSB2
- IC3 pad C9: Net-(IC3-PadC9) -> (no net)
- IC3 pad D11: Net-(IC3-PadD11) -> (no net)
- IC3 pad D6: Net-(IC3-PadD6) -> (no net)
- IC3 pad D7: Net-(IC3-PadD7) -> (no net)
- IC3 pad E10: Net-(IC3-PadE10) -> (no net)
- IC3 pad L4: Net-(IC3-PadL4) -> (no net)
- IC3 pad L8: Net-(IC3-PadL8) -> (no net)
- J2 pad R: Net-(C37-Pad2) -> (no net)
- J5 pad 5: Net-(C72-Pad1) -> SSTX_N
- J5 pad 6: Net-(C73-Pad1) -> SSTX_P
- J5 pad 8: Net-(IC3-PadA3) -> SSRX_P
- J5 pad 9: Net-(IC3-PadA4) -> SSRX_N
- J6 pad 2: Net-(J6-Pad2) -> SPIUSB_D_N
- J6 pad 3: Net-(J6-Pad3) -> SPIUSB_D_P
- J7 pad 2: Net-(J7-Pad2) -> (no net)
- J7 pad SHD: Net-(C107-Pad2) -> /HDMI/HDMI_SHD
- Q1 pad 2: Net-(Q1-Pad2) -> AGND
- Q1 pad 3: +3V3 -> Net-(D1-Pad1)
- Q2 pad 2: Net-(Q2-Pad2) -> AGND
- Q2 pad 3: +3V3 -> Net-(D2-Pad1)
- Q3 pad 1: Net-(Q3-Pad1) -> TEMPO_LED
- Q3 pad 3: Net-(DS1-Pad16) -> (no net)
- Q4 pad 3: Net-(D6-Pad1) -> Net-(DS1-Pad16)
- Q5 pad 3: Net-(D7-Pad1) -> Net-(D6-Pad1)
- R1 pad 1: Net-(D1-Pad2) -> Net-(Q1-Pad1)
- R1 pad 2: Net-(Q1-Pad2) -> CONFIG_DONE
- R10 pad 1: Net-(R10-Pad1) -> GPIF_PCLKT
- R10 pad 2: GD_2 -> GPIF_PCLK
- R11 pad 1: Net-(R11-Pad1) -> GPIF_FLAGAT
- R11 pad 2: GD_6 -> GPIF_FLAGA
- R12 pad 1: Net-(R12-Pad1) -> GD_2T
- R12 pad 2: GD_10 -> GD_2
- R13 pad 1: Net-(R13-Pad1) -> GD_6T
- R13 pad 2: GD_14 -> GD_6
- R14 pad 1: Net-(R14-Pad1) -> GD_10T
- R14 pad 2: GA_1 -> GD_10
- R15 pad 1: Net-(R15-Pad1) -> GD_14T
- R15 pad 2: GD_1 -> GD_14
- R16 pad 1: Net-(R16-Pad1) -> GPIF_SLOE#T
- R16 pad 2: GD_5 -> GPIF_SLOE#
- R17 pad 1: Net-(R17-Pad1) -> GPIF_FLAGBT
- R17 pad 2: GD_9 -> GPIF_FLAGB
- R18 pad 1: Net-(R18-Pad1) -> GD_1T
- R18 pad 2: GD_13 -> GD_1
- R19 pad 1: Net-(R19-Pad1) -> GD_5T
- R19 pad 2: GA_0 -> GD_5
- R2 pad 1: Net-(Q1-Pad1) -> Net-(D1-Pad2)
- R2 pad 2: CONFIG_DONE -> +3V3
- R20 pad 1: Net-(R20-Pad1) -> GD_9T
- R20 pad 2: GD_0 -> GD_9
- R21 pad 1: Net-(R21-Pad1) -> GD_13T
- R21 pad 2: GD_4 -> GD_13
- R22 pad 1: Net-(R22-Pad1) -> GA_1T
- R22 pad 2: GD_8 -> GA_1
- R23 pad 1: Net-(R23-Pad1) -> GPIF_SLRD#T
- R23 pad 2: GD_12 -> GPIF_SLRD#
- R24 pad 1: +1.8V -> GPIF_PKTEND#T
- R24 pad 2: Net-(J1-PadTB) -> GPIF_PKTEND#
- R25 pad 1: JD_IN -> GD_0T
- R25 pad 2: Net-(J1-PadTB) -> GD_0
- R26 pad 1: +1.8V -> GD_4T
- R26 pad 2: Net-(IC1-Pad15) -> GD_4
- R27 pad 1: Net-(J3-PadTB) -> GD_8T
- R27 pad 2: +3V3 -> GD_8
- R28 pad 1: Net-(J4-PadTB) -> GD_12T
- R28 pad 2: +3V3 -> GD_12
- R29 pad 1: Net-(J2-PadRB) -> GA_0T
- R29 pad 2: +3V3 -> GA_0
- R3 pad 1: +1.8V -> Net-(D2-Pad2)
- R3 pad 2: CONFIG_INIT -> +3V3
- R30 pad 1: JD_ROUT -> GPIF_SLWR#T
- R30 pad 2: Net-(J3-PadTB) -> GPIF_SLWR#
- R31 pad 1: JD_LOUT -> GPIF_SLCS#T
- R31 pad 2: Net-(J4-PadTB) -> GPIF_SLCS#
- R32 pad 1: JD_HOUT -> +1.8V
- R32 pad 2: Net-(J2-PadRB) -> Net-(J1-PadTB)
- R33 pad 1: Net-(IC2-Pad15) -> JD_IN
- R33 pad 2: AGND -> Net-(J1-PadTB)
- R34 pad 1: Net-(IC2-Pad16) -> +1.8V
- R34 pad 2: AGND -> Net-(IC1-Pad15)
- R35 pad 1: Net-(R35-Pad1) -> Net-(J3-PadTB)
- R35 pad 2: +1.8V -> +3V3
- R36 pad 1: +1.8V -> Net-(J4-PadTB)
- R36 pad 2: Net-(R36-Pad2) -> +3V3
- R37 pad 1: I2C_SCLK -> Net-(J2-PadRB)
- R37 pad 2: +1.8V -> +3V3
- R38 pad 1: I2C_SDIN -> JD_ROUT
- R38 pad 2: +1.8V -> Net-(J3-PadTB)
- R39 pad 1: +1.8V -> JD_LOUT
- R39 pad 2: Net-(IC3-PadH4) -> Net-(J4-PadTB)
- R4 pad 1: Net-(D2-Pad2) -> CONFIG_INIT
- R4 pad 2: Net-(Q2-Pad2) -> Net-(Q2-Pad1)
- R40 pad 1: Net-(Q3-Pad1) -> JD_HOUT
- R40 pad 2: PWM_LCD_DIM -> Net-(J2-PadRB)
- R41 pad 1: Net-(DS1-Pad15) -> Net-(IC2-Pad15)
- R41 pad 2: +5V -> AGND
- R42 pad 1: CVDDQ -> Net-(IC2-Pad16)
- R42 pad 2: Net-(IC3-PadC5) -> AGND
- R43 pad 1: Net-(IC3-PadC8) -> Net-(R43-Pad1)
- R43 pad 2: AGND -> +1.8V
- R44 pad 1: Net-(IC3-PadB3) -> +1.8V
- R44 pad 2: AGND -> Net-(R44-Pad2)
- R45 pad 1: +1.8V -> I2C_SCLK
- R45 pad 2: RF_SD -> +1.8V
- R46 pad 1: +1.8V -> I2C_SDIN
- R46 pad 2: RF_IRQ -> +1.8V
- R47 pad 1: Net-(Q4-Pad1) -> +1.8V
- R47 pad 2: Net-(R47-Pad2) -> Net-(IC3-PadH4)
- R48 pad 1: Net-(D6-Pad2) -> Net-(Q4-Pad1)
- R48 pad 2: +5V -> PWM_LCD_DIM
- R49 pad 1: Net-(Q5-Pad1) -> Net-(DS1-Pad15)
- R49 pad 2: Net-(R49-Pad2) -> +5V
- R5 pad 1: Net-(Q2-Pad1) -> CONFIG_INIT
- R5 pad 2: CONFIG_INIT -> +1.8V
- R50 pad 1: Net-(D7-Pad2) -> CVDDQ
- R50 pad 2: +5V -> /Cypress FX3/nRESET
- R51 pad 1: Net-(J6-Pad2) -> /Cypress FX3/RUSB2
- R51 pad 2: Net-(R51-Pad2) -> AGND
- R52 pad 1: Net-(J6-Pad3) -> /Cypress FX3/RUSB3
- R52 pad 2: Net-(R52-Pad2) -> AGND
- R53 pad 1: +5V -> +1.8V
- R53 pad 2: USB_FAULT -> RF_SD
- R54 pad 1: +3V3 -> +1.8V
- R54 pad 2: HDMI_SCL -> RF_IRQ
- R55 pad 1: +3V3 -> Net-(Q5-Pad1)
- R55 pad 2: HDMI_SDA -> Net-(R55-Pad2)
- R56 pad 1: Net-(J7-Pad1) -> Net-(D6-Pad2)
- R56 pad 2: AGND -> +5V
- R57 pad 1: AGND -> Net-(Q6-Pad1)
- R57 pad 2: Net-(C107-Pad2) -> Net-(R57-Pad2)
- R58 pad 1: Net-(R58-Pad1) -> Net-(D7-Pad2)
- R58 pad 2: Net-(J7-Pad1) -> +5V
- R59 pad 1: Net-(D8-Pad1) -> +1.8V
- R59 pad 2: +3V3 -> Net-(R59-Pad2)
- R6 pad 1: Net-(R6-Pad1) -> GD_3T
- R60 pad 1: HDMI_5V0 -> SPIUSB_D_P
- R60 pad 2: Net-(C106-Pad1) -> /SPIUSBBRIDGE/SPIUSB_DT_P
- R61 pad 1: Net-(R61-Pad1) -> SPIUSB_D_N
- R61 pad 2: Net-(R61-Pad2) -> /SPIUSBBRIDGE/SPIUSB_DT_N
- R62 pad 1: HDMI_5V0 -> +5V
- R62 pad 2: Net-(J7-Pad17) -> USB_FAULT
- R63 pad 1: HDMI_5V0 -> +3V3
- R63 pad 2: Net-(J7-Pad18) -> HDMI_SCL
- R64 pad 1: Net-(R61-Pad1) -> +3V3
- R64 pad 2: AGND -> HDMI_SDA
- R65 pad 1: +1.8V -> Net-(J7-Pad1)
- R65 pad 2: ENCC0_SW -> AGND
- R66 pad 1: +1.8V -> AGND
- R66 pad 2: ENCC2_SW -> /HDMI/HDMI_SHD
- R67 pad 1: +1.8V -> Net-(R67-Pad1)
- R67 pad 2: Net-(R67-Pad2) -> Net-(J7-Pad1)
- R68 pad 1: +1.8V -> (no net)
- R68 pad 2: Net-(R68-Pad2) -> +3V3
- R69 pad 1: +1.8V -> HDMI_5V0
- R69 pad 2: Net-(R69-Pad2) -> Net-(C106-Pad1)
- R7 pad 1: Net-(R7-Pad1) -> GD_7T
- R70 pad 1: +1.8V -> HDMI_DETECT
- R71 pad 1: ENCC0_Q0 -> HDMI_5V0
- R71 pad 2: Net-(R67-Pad2) -> Net-(J7-Pad17)
- R72 pad 1: ENCC0_Q1 -> HDMI_5V0
- R72 pad 2: Net-(R69-Pad2) -> Net-(J7-Pad18)
- R73 pad 1: ENCC2_Q0 -> HDMI_DETECT
- R73 pad 2: Net-(R68-Pad2) -> AGND
- R74 pad 1: ENCC2_Q1 -> +1.8V
- R74 pad 2: Net-(R70-Pad2) -> ENCC0_SW
- R75 pad 2: ENCC1_SW -> ENCC2_SW
- R76 pad 1: +3V3 -> +1.8V
- R76 pad 2: ENCC3_SW -> Net-(R76-Pad2)
- R78 pad 1: +3V3 -> +1.8V
- R8 pad 1: Net-(R8-Pad1) -> GD_11T
- R80 pad 1: +3V3 -> ENCC0_Q0
- R80 pad 2: Net-(R80-Pad2) -> Net-(R76-Pad2)
- R81 pad 1: ENCC1_Q0 -> ENCC0_Q1
- R81 pad 2: Net-(R77-Pad2) -> Net-(R78-Pad2)
- R82 pad 1: ENCC1_Q1 -> ENCC2_Q0
- R82 pad 2: Net-(R79-Pad2) -> Net-(R77-Pad2)
- R83 pad 1: ENCC3_Q0 -> ENCC2_Q1
- R83 pad 2: Net-(R78-Pad2) -> Net-(R79-Pad2)
- R84 pad 1: ENCC3_Q1 -> +1.8V
- R84 pad 2: Net-(R80-Pad2) -> ENCC1_SW
- R9 pad 1: Net-(R9-Pad1) -> GD_15T
- ROT1 pad A: Net-(R67-Pad2) -> Net-(R76-Pad2)
- ROT1 pad B: Net-(R69-Pad2) -> Net-(R78-Pad2)
- ROT2 pad A: Net-(R68-Pad2) -> Net-(R77-Pad2)
- ROT2 pad B: Net-(R70-Pad2) -> Net-(R79-Pad2)
- ROT3 pad A: Net-(R77-Pad2) -> Net-(R86-Pad2)
- ROT3 pad B: Net-(R79-Pad2) -> Net-(R88-Pad2)
- ROT4 pad A: Net-(R78-Pad2) -> Net-(R87-Pad2)
- ROT4 pad B: Net-(R80-Pad2) -> Net-(R89-Pad2)
- U1 pad A10: Net-(U1-PadA10) -> (no net)
- U1 pad A12: Net-(U1-PadA12) -> (no net)
- U1 pad A13: Net-(U1-PadA13) -> (no net)
- U1 pad A14: Net-(U1-PadA14) -> (no net)
- U1 pad A15: Net-(U1-PadA15) -> (no net)
- U1 pad A2: Net-(U1-PadA2) -> (no net)
- U1 pad A4: Net-(U1-PadA4) -> (no net)
- U1 pad A5: Net-(U1-PadA5) -> (no net)
- U1 pad A8: Net-(U1-PadA8) -> (no net)
- U1 pad A9: Net-(U1-PadA9) -> (no net)
- U1 pad B1: Net-(U1-PadB1) -> (no net)
- U1 pad B10: Net-(U1-PadB10) -> (no net)
- U1 pad B11: Net-(U1-PadB11) -> (no net)
- U1 pad B12: Net-(U1-PadB12) -> (no net)
- U1 pad B14: Net-(U1-PadB14) -> (no net)
- U1 pad B15: Net-(U1-PadB15) -> (no net)
- U1 pad B16: Net-(U1-PadB16) -> (no net)
- U1 pad B2: Net-(U1-PadB2) -> (no net)
- U1 pad B9: Net-(U1-PadB9) -> (no net)
- U1 pad C1: Net-(U1-PadC1) -> (no net)
- U1 pad C11: Net-(U1-PadC11) -> (no net)
- U1 pad C12: Net-(U1-PadC12) -> (no net)
- U1 pad C13: Net-(U1-PadC13) -> (no net)
- U1 pad C14: Net-(U1-PadC14) -> (no net)
- U1 pad C16: Net-(U1-PadC16) -> (no net)
- U1 pad C2: Net-(U1-PadC2) -> (no net)
- U1 pad C3: Net-(U1-PadC3) -> (no net)
- U1 pad C7: Net-(R61-Pad1) -> HDMI_DETECT
- U1 pad C8: Net-(U1-PadC8) -> (no net)
- U1 pad C9: Net-(U1-PadC9) -> (no net)
- U1 pad D1: Net-(U1-PadD1) -> (no net)
- U1 pad D10: Net-(U1-PadD10) -> (no net)
- U1 pad D11: Net-(U1-PadD11) -> (no net)
- U1 pad D13: Net-(U1-PadD13) -> (no net)
- U1 pad D14: Net-(U1-PadD14) -> (no net)
- U1 pad D15: Net-(U1-PadD15) -> (no net)
- U1 pad D16: Net-(U1-PadD16) -> (no net)
- U1 pad D3: Net-(U1-PadD3) -> (no net)
- U1 pad D4: Net-(U1-PadD4) -> (no net)
- U1 pad D6: Net-(U1-PadD6) -> (no net)
- U1 pad D8: Net-(U1-PadD8) -> (no net)
- U1 pad D9: Net-(U1-PadD9) -> (no net)
- U1 pad E1: Net-(U1-PadE1) -> (no net)
- U1 pad E11: Net-(U1-PadE11) -> (no net)
- U1 pad E12: Net-(U1-PadE12) -> (no net)
- U1 pad E13: Net-(U1-PadE13) -> (no net)
- U1 pad E15: Net-(U1-PadE15) -> (no net)
- U1 pad E16: Net-(U1-PadE16) -> (no net)
- U1 pad E2: Net-(U1-PadE2) -> (no net)
- U1 pad E3: Net-(U1-PadE3) -> (no net)
- U1 pad E6: Net-(U1-PadE6) -> (no net)
- U1 pad F12: Net-(U1-PadF12) -> (no net)
- U1 pad F13: Net-(U1-PadF13) -> (no net)
- U1 pad F14: Net-(U1-PadF14) -> (no net)
- U1 pad F15: Net-(U1-PadF15) -> (no net)
- U1 pad F2: Net-(U1-PadF2) -> (no net)
- U1 pad F3: Net-(U1-PadF3) -> (no net)
- U1 pad F4: Net-(U1-PadF4) -> (no net)
- U1 pad G1: Net-(U1-PadG1) -> (no net)
- U1 pad G11: Net-(U1-PadG11) -> (no net)
- U1 pad G12: Net-(U1-PadG12) -> (no net)
- U1 pad G14: Net-(U1-PadG14) -> (no net)
- U1 pad G15: Net-(U1-PadG15) -> (no net)
- U1 pad G16: Net-(U1-PadG16) -> (no net)
- U1 pad G2: Net-(U1-PadG2) -> (no net)
- U1 pad H1: Net-(U1-PadH1) -> (no net)
- U1 pad H11: Net-(U1-PadH11) -> (no net)
- U1 pad H12: Net-(U1-PadH12) -> (no net)
- U1 pad H13: Net-(U1-PadH13) -> (no net)
- U1 pad H14: Net-(U1-PadH14) -> (no net)
- U1 pad H16: Net-(U1-PadH16) -> (no net)
- U1 pad H2: Net-(U1-PadH2) -> (no net)
- U1 pad H3: Net-(U1-PadH3) -> (no net)
- U1 pad H4: Net-(U1-PadH4) -> (no net)
- U1 pad H5: Net-(U1-PadH5) -> (no net)
- U1 pad J1: Net-(U1-PadJ1) -> (no net)
- U1 pad J13: GPIF_FLAGA -> GPIF_FLAGAT
- U1 pad J14: GPIF_FLAGB -> GPIF_FLAGBT
- U1 pad J15: Net-(U1-PadJ15) -> (no net)
- U1 pad J16: Net-(U1-PadJ16) -> (no net)
- U1 pad J3: Net-(U1-PadJ3) -> (no net)
- U1 pad J4: Net-(U1-PadJ4) -> (no net)
- U1 pad J5: Net-(U1-PadJ5) -> (no net)
- U1 pad K1: Net-(U1-PadK1) -> (no net)
- U1 pad K12: GPIF_SLCS# -> GPIF_SLCS#T
- U1 pad K13: Net-(R7-Pad1) -> GD_10T
- U1 pad K15: Net-(R15-Pad1) -> GD_13T
- U1 pad K16: Net-(R20-Pad1) -> GD_11T
- U1 pad K2: Net-(U1-PadK2) -> (no net)
- U1 pad K3: Net-(U1-PadK3) -> (no net)
- U1 pad K5: Net-(U1-PadK5) -> (no net)
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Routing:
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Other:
- copper layers 2 -> 8
- net class Analog added: clearance 0.08, trace_width 0.3, via_dia 0.48, via_drill 0.25
- net class Config added: clearance 0.08, trace_width 0.15, via_dia 0.48, via_drill 0.25
- net class Default: clearance 0.2 -> 0.08; trace_width 0.25 -> 0.15; via_dia 0.6 -> 0.48; via_drill 0.4 -> 0.25
- net class GPIF added: clearance 0.08, trace_width 0.15, via_dia 0.48, via_drill 0.25
- net class HDMI added: clearance 0.08, trace_width 0.15, via_dia 0.48, via_drill 0.25
- net class Peripherals added: clearance 0.08, trace_width 0.15, via_dia 0.48, via_drill 0.25
- net class Power added: clearance 0.08, trace_width 0.3, via_dia 0.48, via_drill 0.25
- net class SSUSB added: clearance 0.08, trace_width 0.15, via_dia 0.48, via_drill 0.25
- net class UI added: clearance 0.08, trace_width 0.15, via_dia 0.48, via_drill 0.25
- net class USB added: clearance 0.08, trace_width 0.15, via_dia 0.48, via_drill 0.25
- rule trace_clearance: 0.2 -> 0.08
- rule trace_min: 0.2 -> 0.0762
- rule via_min_drill: 0.3 -> 0.15
- rule via_min_size: 0.4 -> 0.25

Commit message: jan17review
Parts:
- R32, R33: moved to B.Cu
- moved CON1 186.2 mm to (238.8, 104.1)
- moved R33 93.7 mm to (48.3, 75.6), turned to 180 degrees
- moved J1 48.1 mm to (55.8, 48.3), turned to 90 degrees
- moved R32 39.4 mm to (48.3, 70.2), turned to 180 degrees
- moved SW1 17.4 mm to (86.4, 50.8)
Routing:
- net +1.0V: track 4.24 -> 4.95 mm, vias 6 -> 7
